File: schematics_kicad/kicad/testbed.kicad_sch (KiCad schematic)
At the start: 0 parts

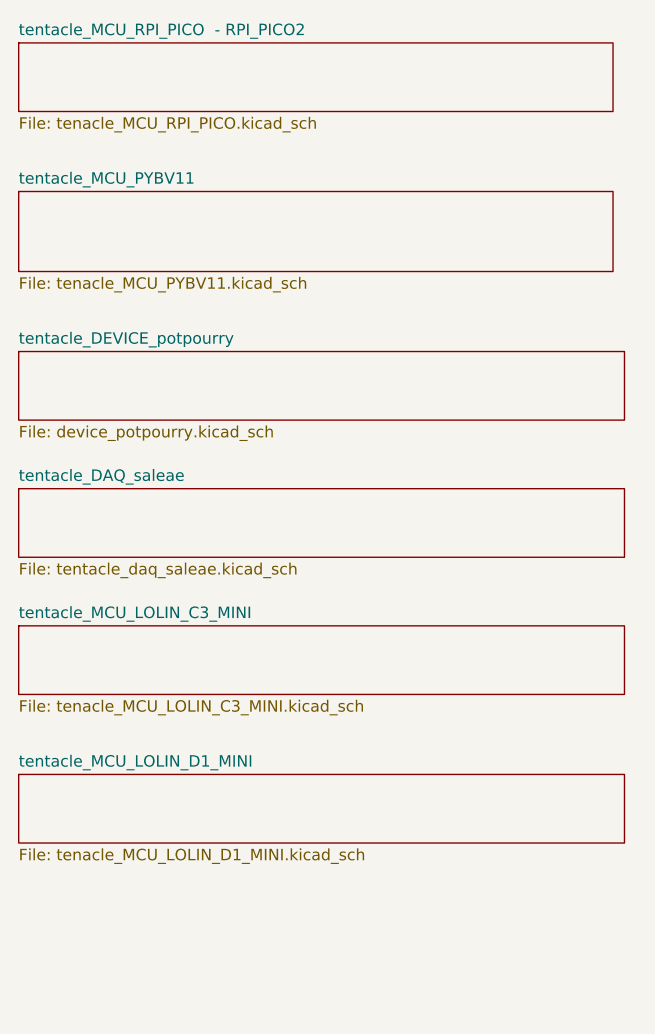
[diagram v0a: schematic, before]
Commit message: Updating schematics for RPI_PICO_W for tentacle v0.4
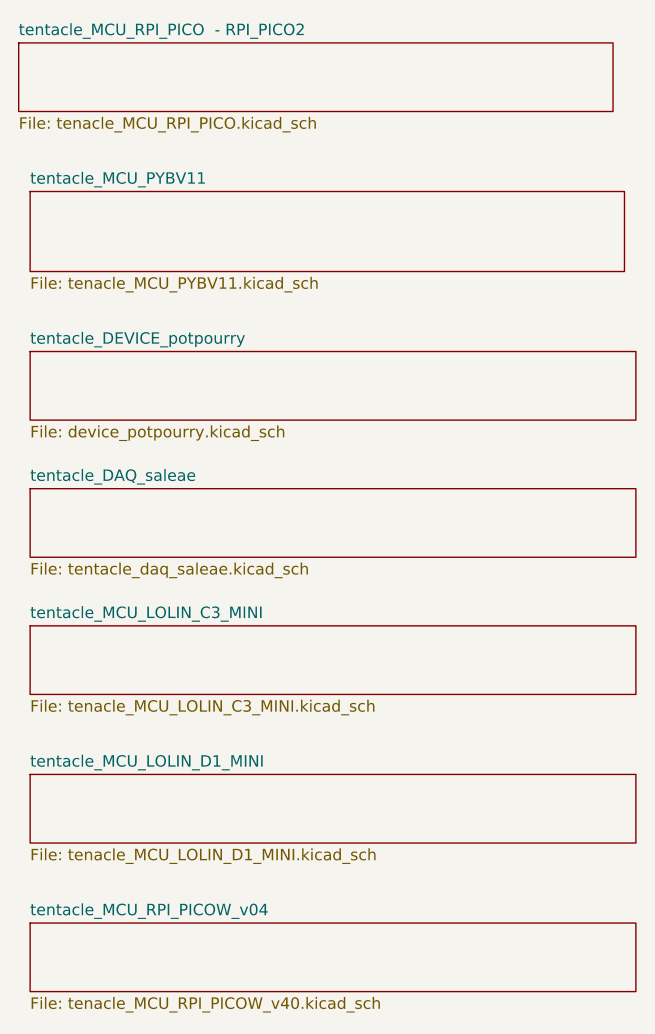
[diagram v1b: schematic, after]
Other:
- added sheet tentacle_MCU_RPI_PICOW_v04 (tenacle_MCU_RPI_PICOW_v40.kicad_sch)
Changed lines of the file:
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@@
 	)
 	(sheet
-		(at 36.83 82.55)
+		(at 38.1 82.55)
 		(size 67.31 7.62)
 		(fields_autoplaced yes)
@@
 		)
 		(property "Sheetname" "tentacle_DAQ_saleae"
-			(at 36.83 81.8384 0)
+			(at 38.1 81.8384 0)
 			(effects
 				(font
@@
 		)
 		(property "Sheetfile" "tentacle_daq_saleae.kicad_sch"
-			(at 36.83 90.7546 0)
+			(at 38.1 90.7546 0)
 			(effects
 				(font
@@
 				(path "/188054c4-74b7-429a-b3f5-c6f3151e27de"
 					(page "5")
+				)
+			)
+		)
+	)
+	(sheet
+		(at 38.1 130.81)
+		(size 67.31 7.62)
+		(fields_autoplaced yes)
+		(stroke
+			(width 0.1524)
+			(type solid)
+		)
+		(fill
+			(color 0 0 0 0.0000)
+		)
+		(property "Sheetname" "tentacle_MCU_RPI_PICOW_v04"
+			(at 38.1 130.0984 0)
+			(effects
+				(font
+					(size 1.27 1.27)
+				)
+				(justify left bottom)
+			)
+		)
+		(property "Sheetfile" "tenacle_MCU_RPI_PICOW_v40.kicad_sch"
+			(at 38.1 139.0146 0)
+			(effects
+				(font
+					(size 1.27 1.27)
+				)
+				(justify left top)
+			)
+		)
+		(instances
+			(project "testbed"
+				(path "/188054c4-74b7-429a-b3f5-c6f3151e27de"
+					(page "17")
 				)
 			)
@@
 	)
 	(sheet
-		(at 36.83 49.53)
+		(at 38.1 49.53)
 		(size 66.04 8.89)
 		(fields_autoplaced yes)
@@
 		)
 		(property "Sheetname" "tentacle_MCU_PYBV11"
-			(at 36.83 48.8184 0)
+			(at 38.1 48.8184 0)
 			(effects
 				(font
@@
 		)
 		(property "Sheetfile" "tenacle_MCU_PYBV11.kicad_sch"
-			(at 36.83 59.0046 0)
+			(at 38.1 59.0046 0)
 			(effects
 				(font
@@
 	)
 	(sheet
-		(at 36.83 114.3)
+		(at 38.1 114.3)
 		(size 67.31 7.62)
 		(fields_autoplaced yes)
@@
 		)
 		(property "Sheetname" "tentacle_MCU_LOLIN_D1_MINI"
-			(at 36.83 113.5884 0)
+			(at 38.1 113.5884 0)
 			(effects
 				(font
@@
 		)
 		(property "Sheetfile" "tenacle_MCU_LOLIN_D1_MINI.kicad_sch"
-			(at 36.83 122.5046 0)
+			(at 38.1 122.5046 0)
 			(effects
 				(font
@@
 	)
 	(sheet
-		(at 36.83 67.31)
+		(at 38.1 67.31)
 		(size 67.31 7.62)
 		(fields_autoplaced yes)
@@
 		)
 		(property "Sheetname" "tentacle_DEVICE_potpourry"
-			(at 36.83 66.5984 0)
+			(at 38.1 66.5984 0)
 			(effects
 				(font
@@
 		)
 		(property "Sheetfile" "device_potpourry.kicad_sch"
-			(at 36.83 75.5146 0)
+			(at 38.1 75.5146 0)
 			(effects
 				(font
@@
 	)
 	(sheet
-		(at 36.83 97.79)
+		(at 38.1 97.79)
 		(size 67.31 7.62)
 		(fields_autoplaced yes)
@@
 		)
 		(property "Sheetname" "tentacle_MCU_LOLIN_C3_MINI"
-			(at 36.83 97.0784 0)
+			(at 38.1 97.0784 0)
 			(effects
 				(font
@@
 		)
 		(property "Sheetfile" "tenacle_MCU_LOLIN_C3_MINI.kicad_sch"
-			(at 36.83 105.9946 0)
-			(effects
-				(font
+			(at 38.1 105.9946 0)
+			(effects
+				(font
